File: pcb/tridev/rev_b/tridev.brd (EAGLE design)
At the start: 108 x 72.4 mm, 66 parts, among them J1 MICRO_USB_B_HIROSE_ZX62R-B-5P, J5 TC2030-JLINK-L, J6 TC2030-JLINK-L, U1 TRIPOINT-BREAKOUT, U2 NRF51822QF, U3 MAX8887EZK33+T, U4 FT232HQ, X1 EPSON-FA-128, X2 TXC-8Z-12MHZ

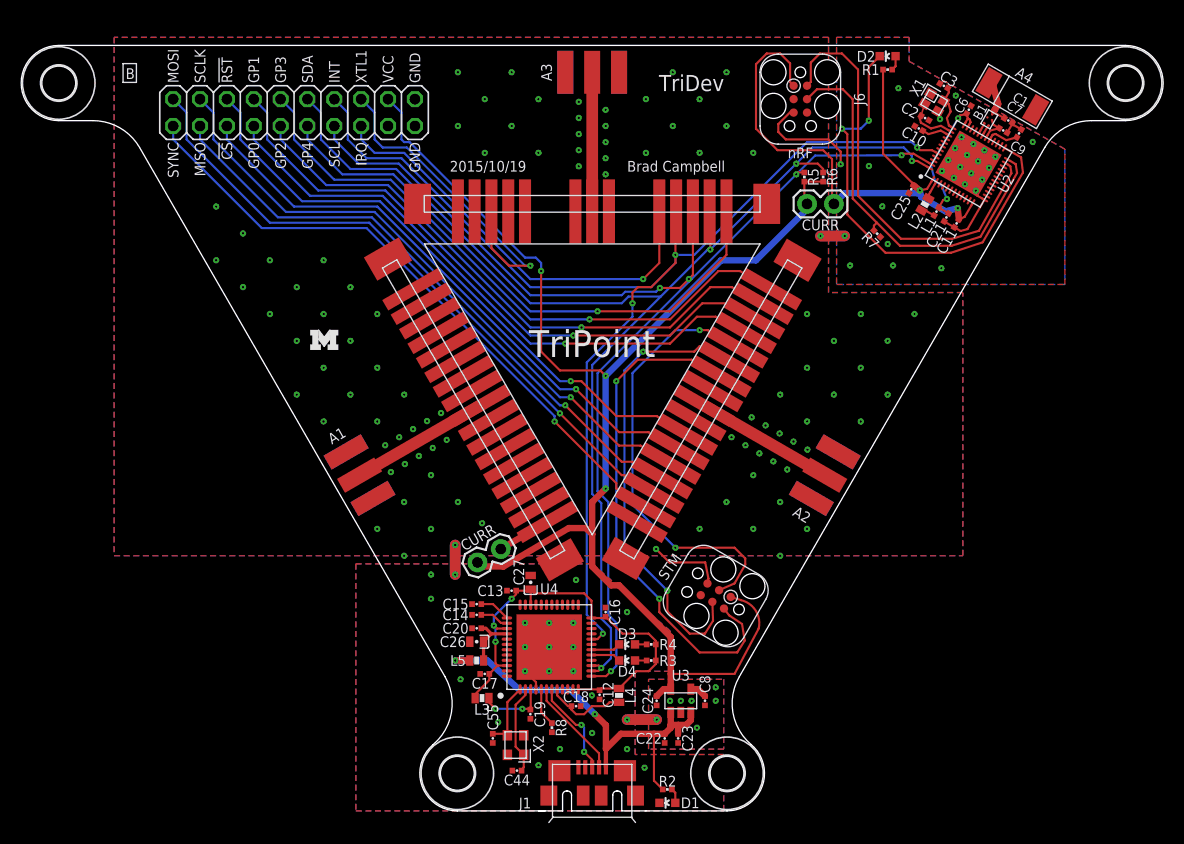
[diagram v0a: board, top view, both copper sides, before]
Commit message: update tridev with more jumpers
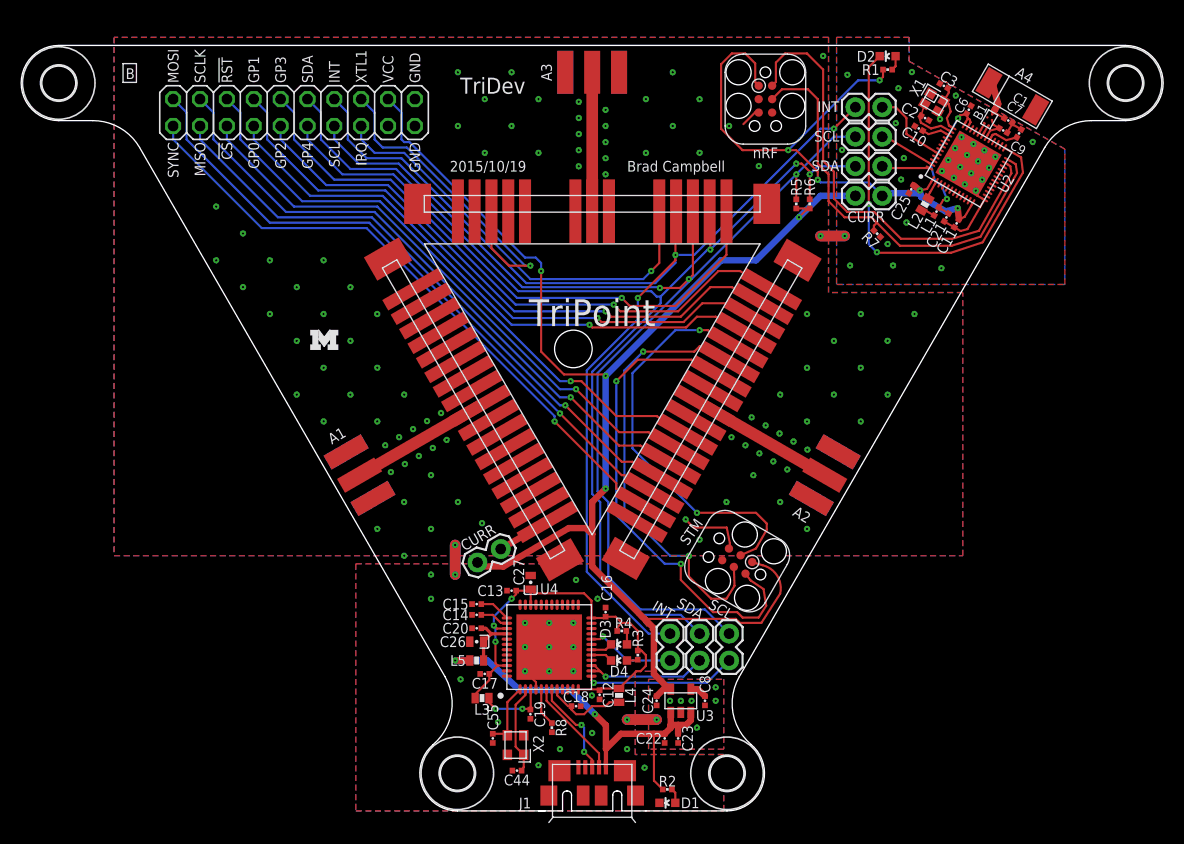
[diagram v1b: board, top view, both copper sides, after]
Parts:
- added J11, J12, J13, J7, J8, J9: (no value), SparkFun-Passives:1X02
- moved J3 4.64 mm to (24.9, 13.7)
- moved J5 3.88 mm to (13.7, -20.8)
- moved J6 3.30 mm to (16.4, 22.9)
- moved R4 3.07 mm to (2.79, -27.4), turned to 180 degrees
- moved R6 2.84 mm to (20.6, 13.0)
- moved R5 2.65 mm to (19.3, 13.0)
- moved R3 1.37 mm to (4.32, -29.7), turned to 90 degrees
- moved D3 0.76 mm to (2.54, -28.7)
- moved D4 0.76 mm to (2.54, -30.2)
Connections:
- new net I2C_SCL_FTDI: J11.1, U4.13
- new net I2C_SCL_NRF: J7.1, U2.47
- new net I2C_SDA_FTDI: J12.2, U4.14, U4.15
- new net I2C_SDA_NRF: J8.2, U2.48
- new net TP_INT_FTDI: J13.2, U4.20
- new net TP_INT_NRF: J9.2, U2.44
- net I2C_SCL: now also J11.2, J7.2; no longer U2.47, U4.13
- net I2C_SDA: now also J12.1, J8.1; no longer U2.48, U4.14, U4.15
- net TP_INT: now also J13.1, J9.1; no longer U2.44, U4.20
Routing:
- net I2C_SCL_FTDI: track 0.00 -> 14.4 mm, vias 0 -> 1
- net I2C_SDA_FTDI: track 0.00 -> 12.1 mm, vias 0 -> 1
- net GND: track 44.7 -> 35.2 mm, vias 154 -> 156
- net I2C_SDA: track 123.1 -> 114.3 mm, vias 4 -> 3
- net TP_INT_FTDI: track 0.00 -> 8.49 mm, vias 0 -> 1
- net TP_INT_NRF: track 0.00 -> 7.73 mm
- net VCC: track 130.5 -> 137.0 mm, vias 3 -> 4
- net I2C_SCL_NRF: track 0.00 -> 5.43 mm
- net TP_INT: track 118.5 -> 113.2 mm, vias 4 -> 3
- net I2C_SDA_NRF: track 0.00 -> 4.53 mm
- net I2C_SCL: track 120.9 -> 117.0 mm, vias 5 -> 3
- net SWDIO/!RESET: track 40.4 -> 43.3 mm
- net SWDCLK: track 38.1 -> 40.9 mm
- net N$6: track 43.0 -> 40.3 mm
- net N$8: track 41.5 -> 39.0 mm
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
